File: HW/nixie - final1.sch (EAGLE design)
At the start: 17 parts, among them IC1 74141N, IC2 74141N, IC3 74141N, IC4 74141N, IC7 74HC595N, IC8 74HC595N

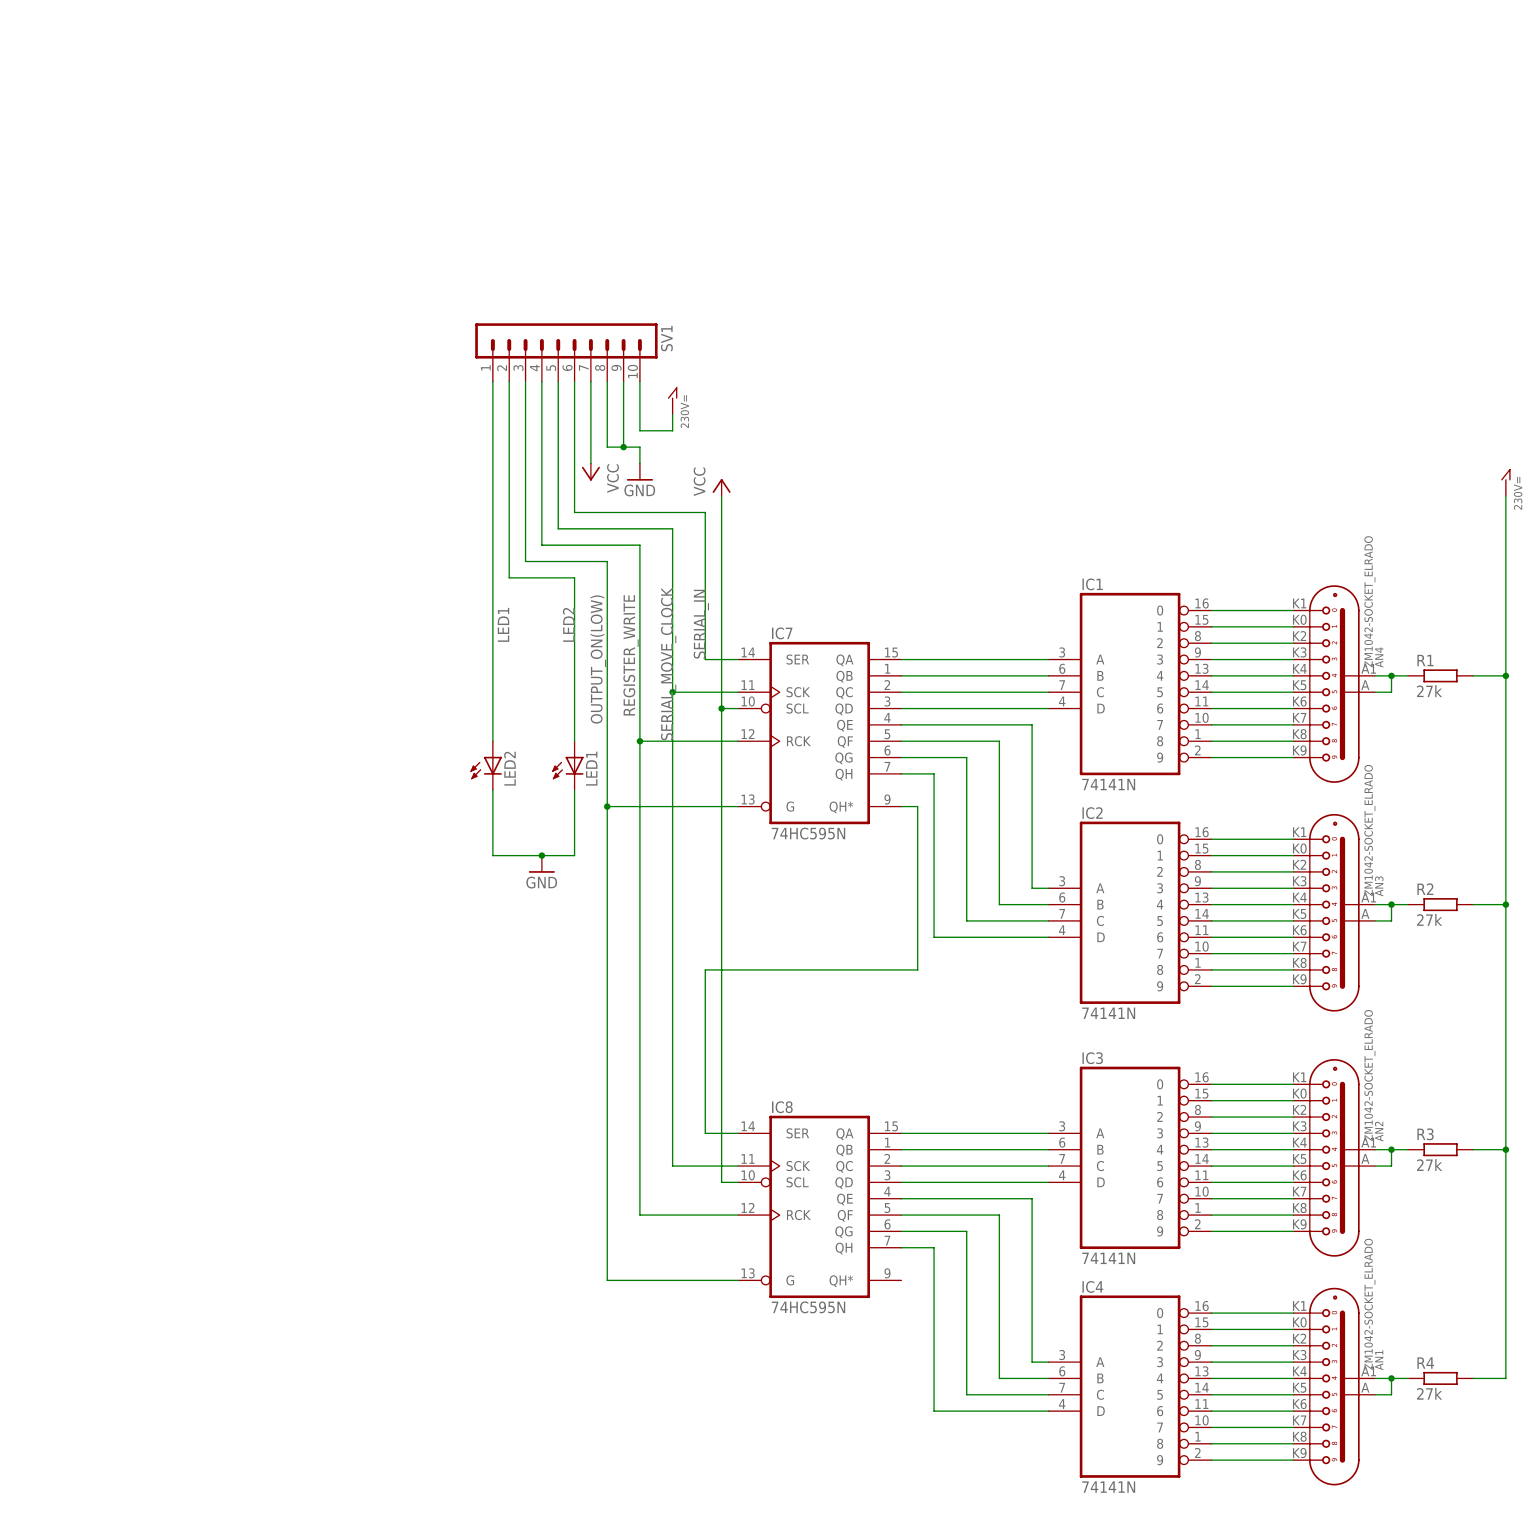
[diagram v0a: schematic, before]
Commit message: Update HW, SW - hlavne SW blizke HW, hodiny funkcni, bezi testovaci sekvence, na zmacknuti tlacitka se zobrazi
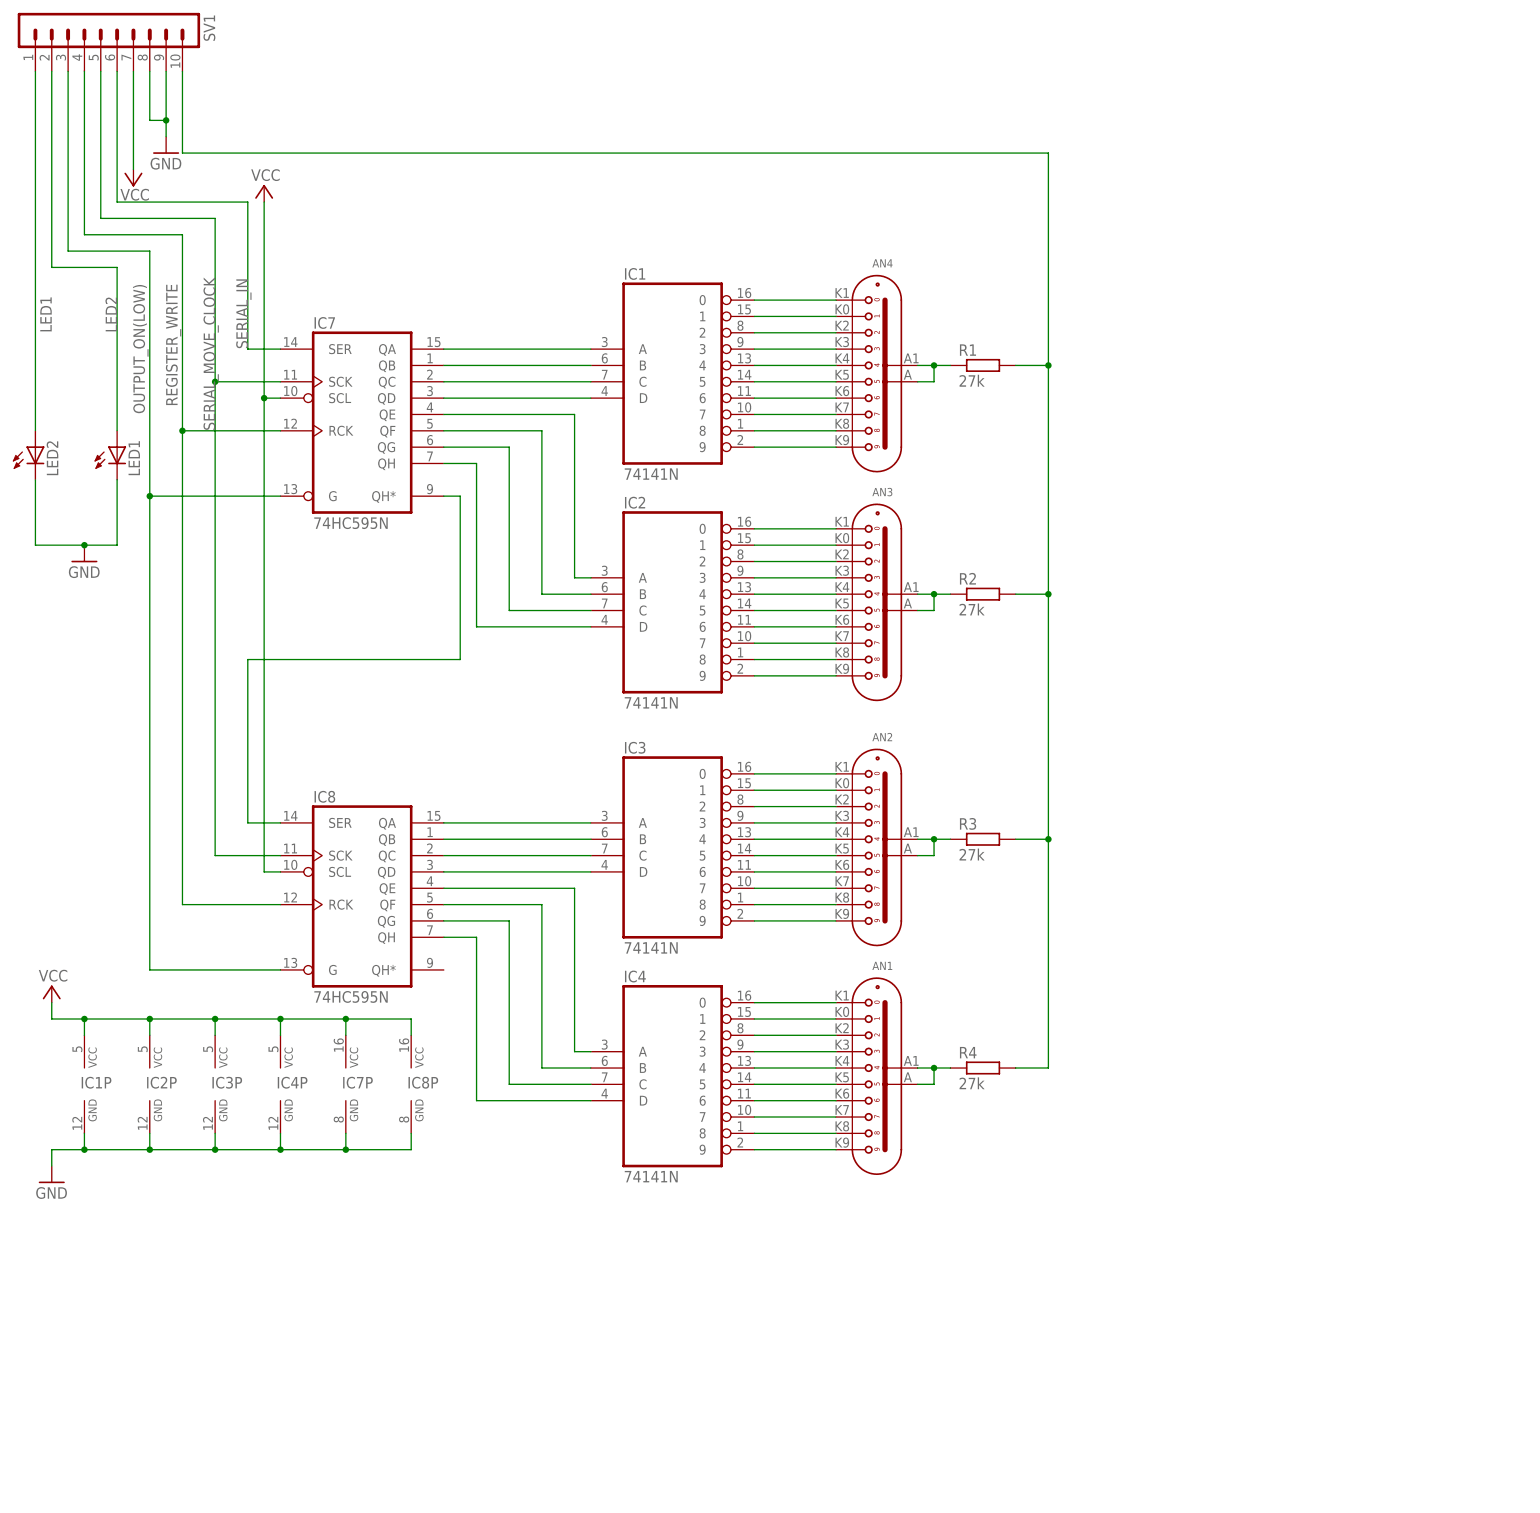
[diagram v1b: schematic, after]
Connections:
- net 230V= renamed N$41
- net GND: now also IC1P.GND, IC2P.GND, IC3P.GND, IC4P.GND, IC7P.GND, IC8P.GND
- net VCC: now also IC1P.VCC, IC2P.VCC, IC3P.VCC, IC4P.VCC, IC7P.VCC, IC8P.VCC
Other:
- moved on the sheet: AN1, AN2, AN3, AN4, IC1, IC2, IC3, IC4, IC7, IC8, LED1, LED2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
